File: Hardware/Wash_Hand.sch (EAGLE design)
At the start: 89 parts, among them IC1 LM358D, IC2 LP298XS, IC3 405016TSSOP, J1 I2C, J2 ICSP, J3 SPI, J4 9V_CONN, J5 EXT_VCC, J6 6_PIN_SERIAL_CABLEPTH, J8 2X6 FEMALE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

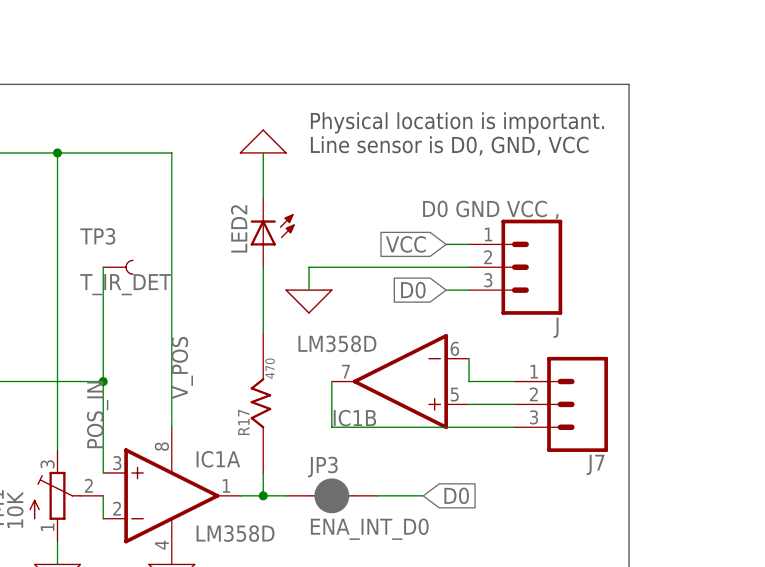
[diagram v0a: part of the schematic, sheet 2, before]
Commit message: Board/Schematic: Update libraries and update values for
some of the components.

Signed-off-by: Konrad Rzeszutek Wilk <konrad@kernel.org>
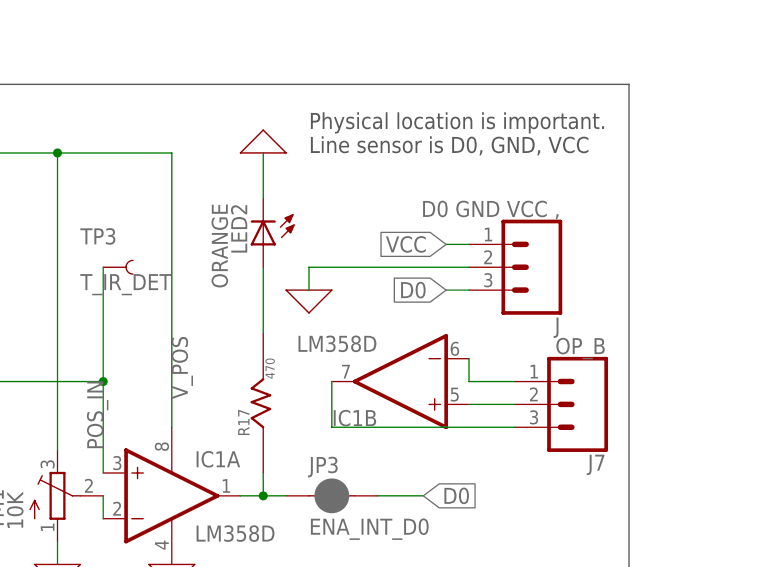
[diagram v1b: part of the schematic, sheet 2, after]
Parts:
- J7: value (none) -> OP_B
- LED2: value (none) -> ORANGE
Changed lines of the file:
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@@
 <layers>
 <layer number="1" name="Top" color="4" fill="1" visible="no" active="no"/>
+<layer number="2" name="Route2" color="1" fill="3" visible="no" active="no"/>
+<layer number="3" name="Route3" color="4" fill="3" visible="no" active="no"/>
+<layer number="4" name="Route4" color="1" fill="4" visible="no" active="no"/>
+<layer number="5" name="Route5" color="4" fill="4" visible="no" active="no"/>
+<layer number="6" name="Route6" color="1" fill="8" visible="no" active="no"/>
+<layer number="7" name="Route7" color="4" fill="8" visible="no" active="no"/>
+<layer number="8" name="Route8" color="1" fill="2" visible="no" active="no"/>
+<layer number="9" name="Route9" color="4" fill="2" visible="no" active="no"/>
+<layer number="10" name="Route10" color="1" fill="7" visible="no" active="no"/>
+<layer number="11" name="Route11" color="4" fill="7" visible="no" active="no"/>
+<layer number="12" name="Route12" color="1" fill="5" visible="no" active="no"/>
+<layer number="13" name="Route13" color="4" fill="5" visible="no" active="no"/>
+<layer number="14" name="Route14" color="1" fill="6" visible="no" active="no"/>
+<layer number="15" name="Route15" color="4" fill="6" visible="no" active="no"/>
 <layer number="16" name="Bottom" color="1" fill="1" visible="no" active="no"/>
 <layer number="17" name="Pads" color="2" fill="1" visible="no" active="no"/>
@@
 <part name="R16" library="darnok_common" deviceset="RESISTOR" device="R1206" value="1K"/>
 <part name="R17" library="darnok_common" deviceset="RESISTOR" device="R1206" value="470"/>
-<part name="LED2" library="adafruit" library_urn="urn:adsk.eagle:library:420" deviceset="LED" device="SMT1206" package3d_urn="urn:adsk.eagle:package:6240349/1"/>
+<part name="LED2" library="adafruit" library_urn="urn:adsk.eagle:library:420" deviceset="LED" device="SMT1206" package3d_urn="urn:adsk.eagle:package:6240349/1" value="ORANGE"/>
 <part name="X_31" library="ngspice-simulation" library_urn="urn:adsk.eagle:library:527439" deviceset="GND" device=""/>
 <part name="R18" library="darnok_common" deviceset="RESISTOR" device="R1206" value="100K"/>
@@
 <part name="C16" library="SparkFun-Capacitors" library_urn="urn:adsk.eagle:library:510" deviceset="10UF" device="-1206-6.3V-20%" package3d_urn="urn:adsk.eagle:package:37426/1" value="0.1uF"/>
 <part name="X_36" library="ngspice-simulation" library_urn="urn:adsk.eagle:library:527439" deviceset="GND" device=""/>
-<part name="J7" library="SparkFun-Connectors" library_urn="urn:adsk.eagle:library:513" deviceset="CONN_03" device="" package3d_urn="urn:adsk.eagle:package:38063/1"/>
+<part name="J7" library="SparkFun-Connectors" library_urn="urn:adsk.eagle:library:513" deviceset="CONN_03" device="" package3d_urn="urn:adsk.eagle:package:38063/1" value="OP_B"/>
 <part name="T1" library="zetex" library_urn="urn:adsk.eagle:library:418" deviceset="PNPSOT23" device="" package3d_urn="urn:adsk.eagle:package:30981/1" value="PNP"/>
 <part name="J8" library="SparkFun-Connectors" library_urn="urn:adsk.eagle:library:513" deviceset="CONN_06X2" device="PTH_FEMALE" package3d_urn="urn:adsk.eagle:package:38277/1" value="2X6 FEMALE"/>

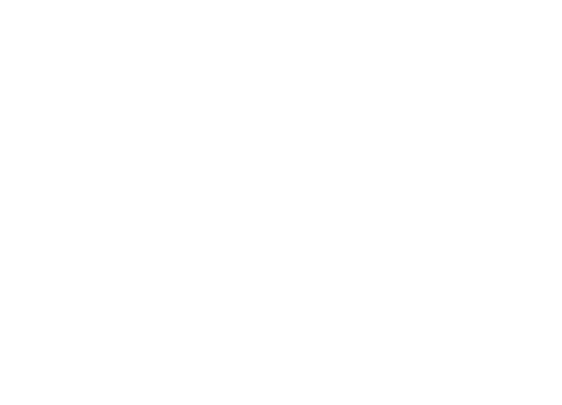
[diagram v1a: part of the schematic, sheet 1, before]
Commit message: Board/Schematic: Add HAPPY_FACE logo
.. because 2021 is right around the corner!

Signed-off-by: Konrad Rzeszutek Wilk <konrad@kernel.org>
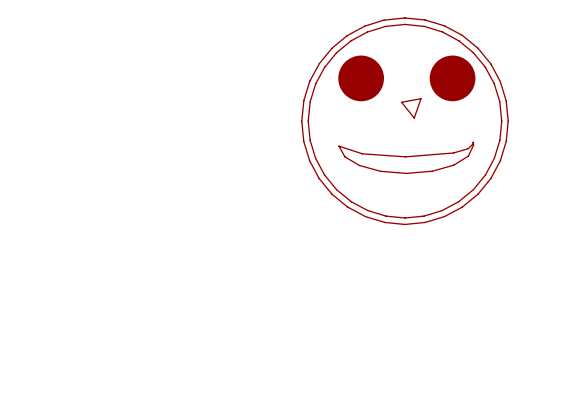
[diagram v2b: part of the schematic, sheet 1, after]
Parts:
- added LOGO2: HAPPY_FACE_LOGO, darnok_logo:HAPPY_FACE_LOGO
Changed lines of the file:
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@@
 <part name="J8" library="SparkFun-Connectors" library_urn="urn:adsk.eagle:library:513" deviceset="CONN_06X2" device="PTH_FEMALE" package3d_urn="urn:adsk.eagle:package:38277/1" value="2X6 FEMALE"/>
 <part name="R12" library="darnok_common" deviceset="RESISTOR" device="R1206" value="1.2K"/>
+<part name="LOGO2" library="darnok_logo" deviceset="HAPPY_FACE_LOGO" device=""/>
 </parts>
 <sheets>
@@
 <attribute name="NAME" x="214.63" y="127.508" size="1.778" layer="95" font="vector"/>
 </instance>
+<instance part="LOGO2" gate="G$1" x="241.3" y="198.12" smashed="yes"/>
 </instances>
 <busses>

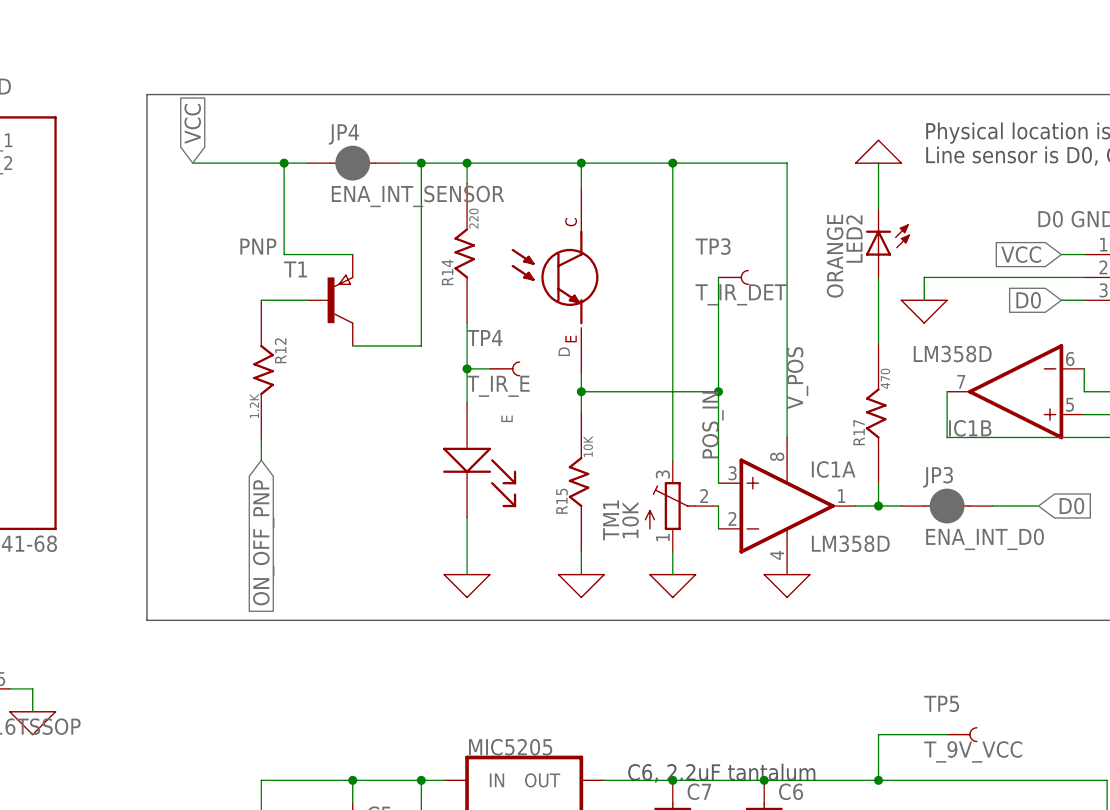
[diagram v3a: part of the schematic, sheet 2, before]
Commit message: Board/Design: Replace PNP with NPN
And also re-route the ground since the NPN will now
control whether this whole thing is going to be on/off.

Signed-off-by: Konrad Rzeszutek Wilk <konrad@kernel.org>
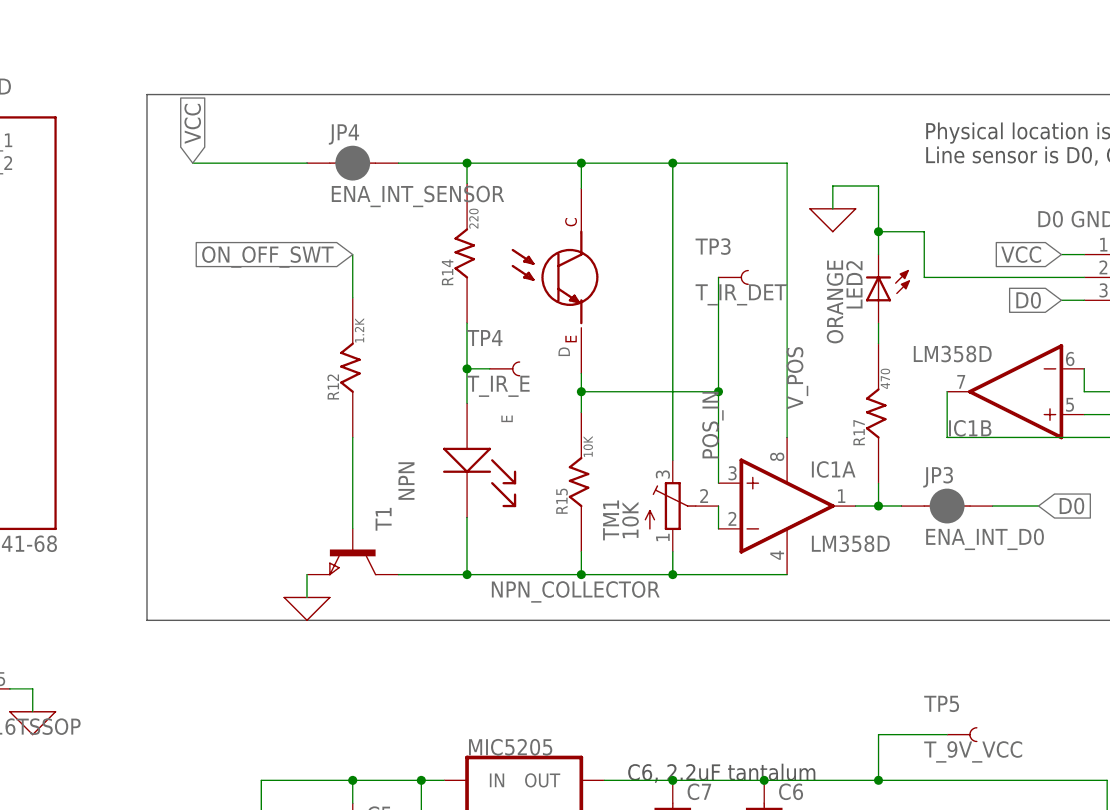
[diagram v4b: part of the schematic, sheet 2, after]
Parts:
- T1: value PNP -> NPN; device zetex:PNPSOT23 -> zetex:NPNSOT23
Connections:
- net ON_OFF_PNP renamed ON_OFF_SWT
- new net NPN_COLLECTOR: E.K$1, IC1P.V-, R15.R_1, T1.C, TM1.A
- net 0: now also T1.E; no longer E.K$1, IC1P.V-, R15.R_1, TM1.A
- net VCC: no longer T1.E
- net V_POS: no longer T1.C
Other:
- moved on the sheet: LED2, R12, T1

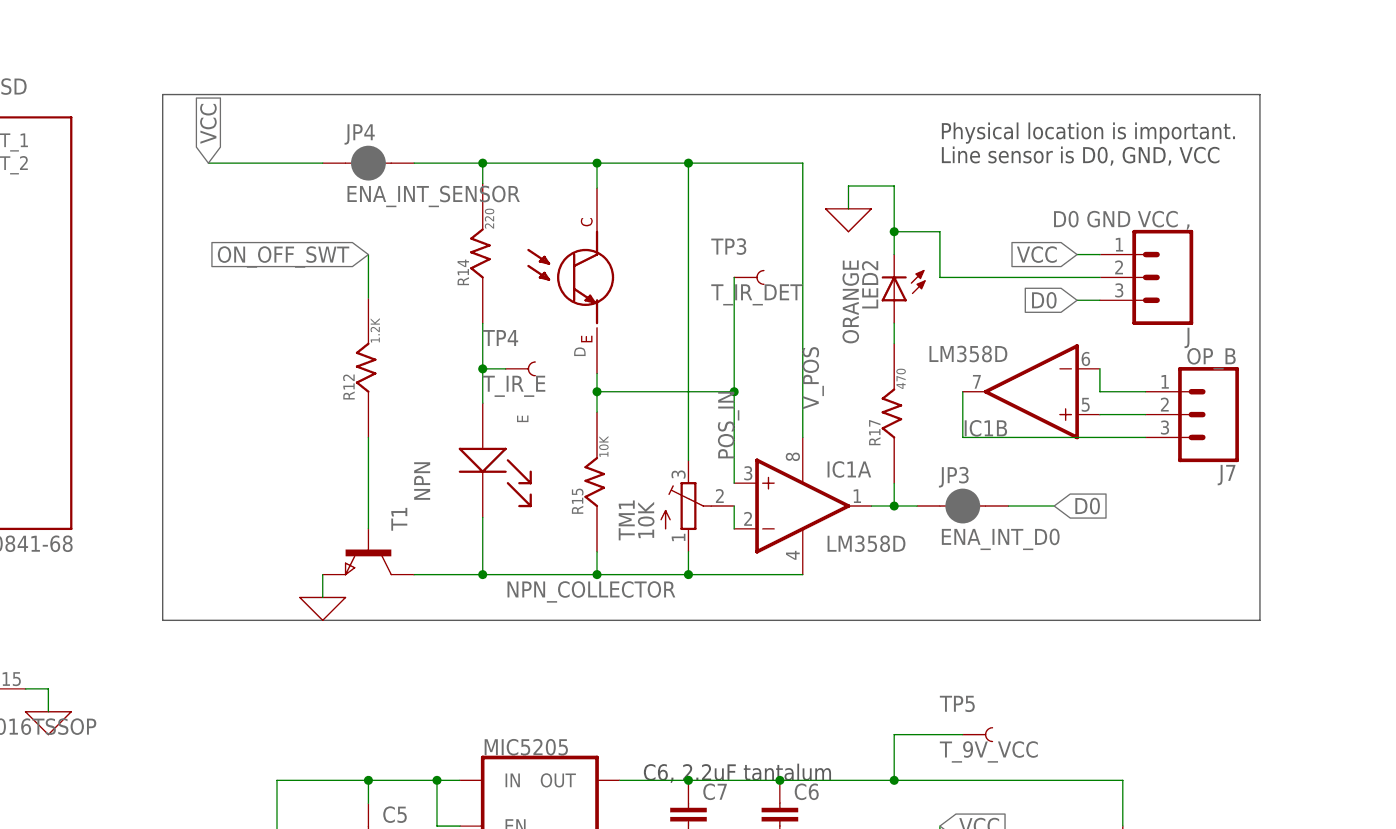
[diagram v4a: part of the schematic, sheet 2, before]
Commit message: Board/Schematic: Add BYPASS_SWITCH
In case we do not want to use the NPN transistor.

Signed-off-by: Konrad Rzeszutek Wilk <konrad@kernel.org>
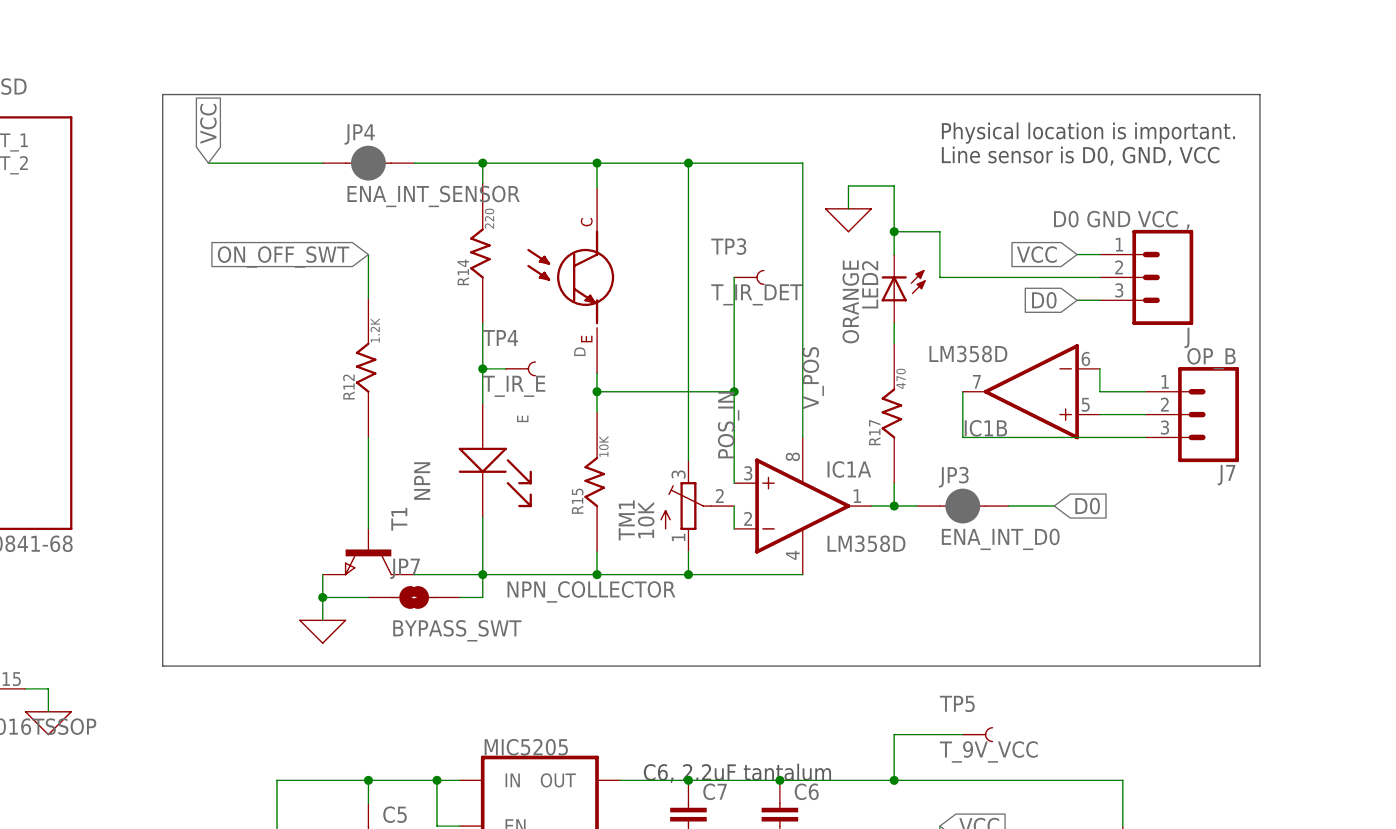
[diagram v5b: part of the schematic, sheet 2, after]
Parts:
- added JP7: BYPASS_SWT, SparkFun-Jumpers:JUMPER-SMT_2_NO_SILK
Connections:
- net 0: now also JP7.1
- net NPN_COLLECTOR: now also JP7.2
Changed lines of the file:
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@@
 <part name="X_1" library="ngspice-simulation" library_urn="urn:adsk.eagle:library:527439" deviceset="GND" device=""/>
 <part name="X_4" library="ngspice-simulation" library_urn="urn:adsk.eagle:library:527439" deviceset="GND" device=""/>
+<part name="JP7" library="SparkFun-Jumpers" library_urn="urn:adsk.eagle:library:528" deviceset="JUMPER-SMT_2_NO" device="_SILK" package3d_urn="urn:adsk.eagle:package:39279/1" value="BYPASS_SWT"/>
 </parts>
 <sheets>
@@
 Line sensor is D0, GND, VCC</text>
 <wire x1="119.38" y1="177.8" x2="241.3" y2="177.8" width="0.1524" layer="97"/>
-<wire x1="241.3" y1="177.8" x2="241.3" y2="119.38" width="0.1524" layer="97"/>
-<wire x1="241.3" y1="119.38" x2="119.38" y2="119.38" width="0.1524" layer="97"/>
-<wire x1="119.38" y1="119.38" x2="119.38" y2="177.8" width="0.1524" layer="97"/>
+<wire x1="241.3" y1="177.8" x2="241.3" y2="114.3" width="0.1524" layer="97"/>
+<wire x1="241.3" y1="114.3" x2="119.38" y2="114.3" width="0.1524" layer="97"/>
+<wire x1="119.38" y1="114.3" x2="119.38" y2="177.8" width="0.1524" layer="97"/>
 <text x="187.96" y="78.74" size="1.778" layer="97">The jumper is if you want to use USB or 9V.
 By default USB is used.</text>
@@
 <attribute name="VALUE" x="143.51" y="150.114" size="1.016" layer="96" rot="R90"/>
 </instance>
-<instance part="X_1" gate="G$1" x="137.16" y="121.92" smashed="yes"/>
+<instance part="X_1" gate="G$1" x="137.16" y="119.38" smashed="yes"/>
 <instance part="X_4" gate="G$1" x="195.58" y="165.1" smashed="yes"/>
+<instance part="JP7" gate="G$1" x="147.32" y="121.92" smashed="yes">
+<attribute name="NAME" x="144.78" y="124.46" size="1.778" layer="95" font="vector"/>
+<attribute name="VALUE" x="144.78" y="119.38" size="1.778" layer="96" font="vector" align="top-left"/>
+</instance>
 </instances>
 <busses>
@@
 <pinref part="X_1" gate="G$1" pin="0"/>
 <wire x1="137.16" y1="124.46" x2="137.16" y2="121.92" width="0.1524" layer="91"/>
+<pinref part="JP7" gate="G$1" pin="1"/>
+<wire x1="137.16" y1="121.92" x2="137.16" y2="119.38" width="0.1524" layer="91"/>
+<wire x1="142.24" y1="121.92" x2="137.16" y2="121.92" width="0.1524" layer="91"/>
+<junction x="137.16" y="121.92"/>
 </segment>
 <segment>
@@
 <wire x1="147.32" y1="124.46" x2="154.94" y2="124.46" width="0.1524" layer="91"/>
 <label x="157.48" y="121.92" size="1.778" layer="95"/>
-</segment>
-</net>
+<pinref part="JP7" gate="G$1" pin="2"/>
+<wire x1="152.4" y1="121.92" x2="154.94" y2="121.92" width="0.1524" layer="91"/>
+<wire x1="154.94" y1="121.92" x2="154.94" y2="124.46" width="0.1524" layer="91"/>
+</segment>
+</net>
